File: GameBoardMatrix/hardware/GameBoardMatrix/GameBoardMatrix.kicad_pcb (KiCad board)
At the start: 2 copper layers, 1 part

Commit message: Started on PCB/Schematic Design
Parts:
- removed C1: C, ECE445L:C_Axial_200mil
- added J1: RPI_5_HeaderPins, Connector_PinSocket_2.54mm:PinSocket_2x20_P2.54mm_Vertical, F.Cu at (32.6, 51.2)
- added U1: MUX1, 8to1_MUX:D16, F.Cu at (129.0, 48.4)
- added U2: MUX1, 8to1_MUX:D16, F.Cu at (137.8, 48.4)
- added U3: MUX1, 8to1_MUX:D16, F.Cu at (146.5, 48.4)
- added U4: MUX1, 8to1_MUX:D16, F.Cu at (155.3, 48.4)
- added U5: MUX1, 8to1_MUX:D16, F.Cu at (164.0, 48.4)
- added U6: A3144, A3144HallEffect:1x03_P1.50mm_Vertical_A3144HallEffect, F.Cu at (141.2, 64.2)
- added U7: A3144, A3144HallEffect:1x03_P1.50mm_Vertical_A3144HallEffect, F.Cu at (141.2, 73.0)
- added U8: A3144, A3144HallEffect:1x03_P1.50mm_Vertical_A3144HallEffect, F.Cu at (141.4, 81.5)

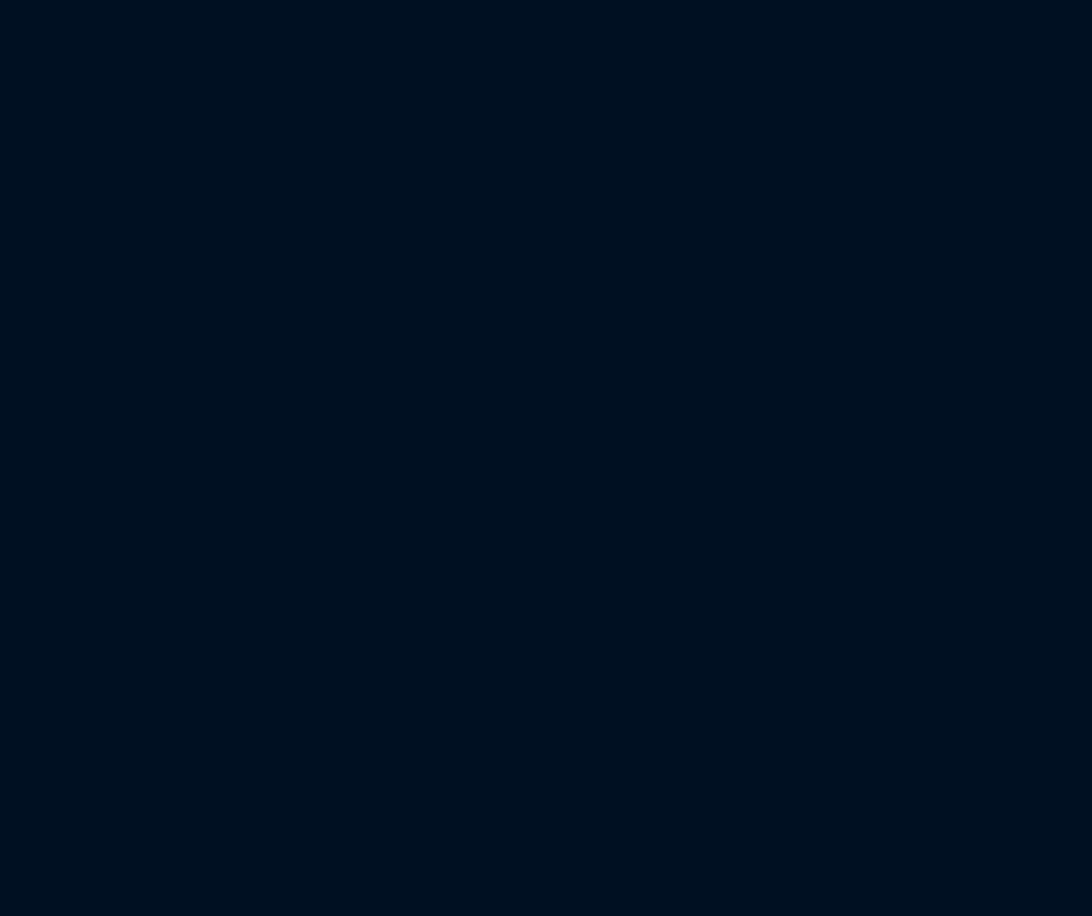
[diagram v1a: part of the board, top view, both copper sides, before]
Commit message: Finished most of the schematic
Still need to tie outputs to gpio pins
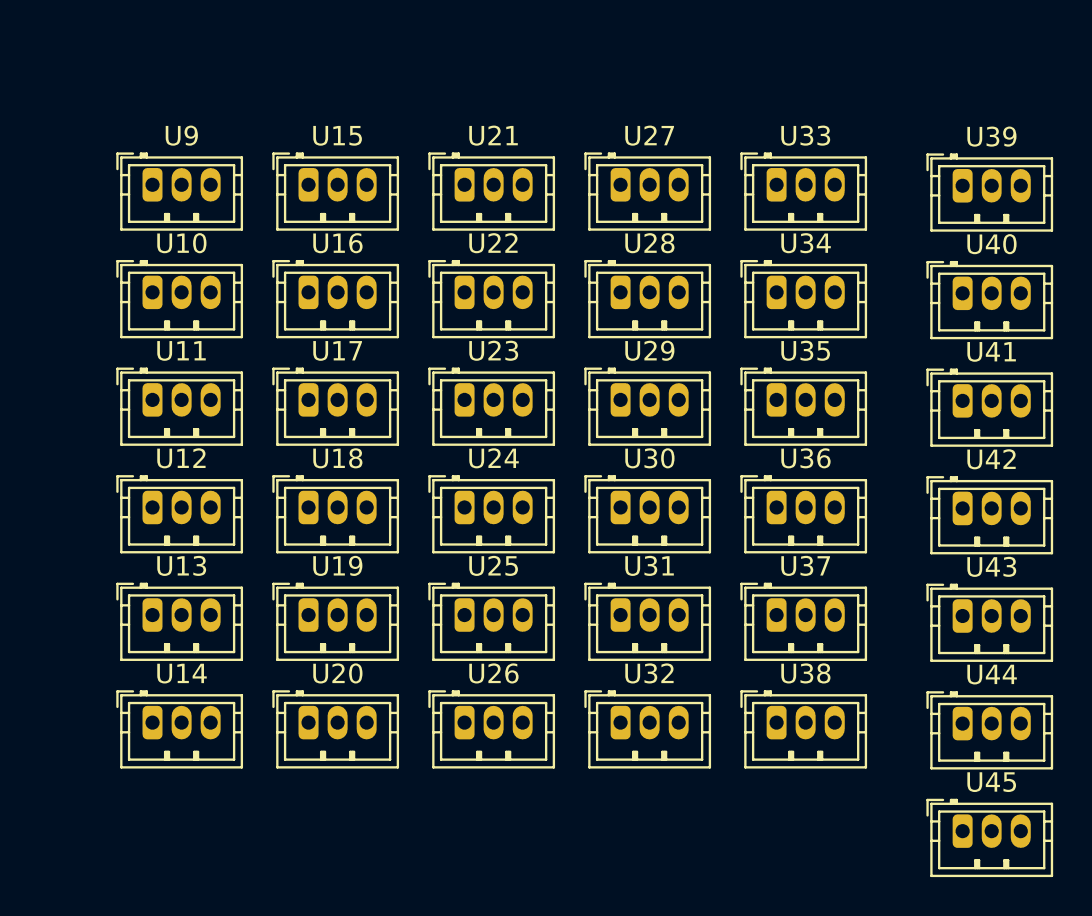
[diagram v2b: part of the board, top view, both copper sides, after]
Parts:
- added U10: A3144, A3144HallEffect:1x03_P1.50mm_Vertical_A3144HallEffect, F.Cu at (172.4, 73.0)
- added U11: A3144, A3144HallEffect:1x03_P1.50mm_Vertical_A3144HallEffect, F.Cu at (172.4, 78.5)
- added U12: A3144, A3144HallEffect:1x03_P1.50mm_Vertical_A3144HallEffect, F.Cu at (172.4, 84.1)
- added U13: A3144, A3144HallEffect:1x03_P1.50mm_Vertical_A3144HallEffect, F.Cu at (172.4, 89.7)
- added U14: A3144, A3144HallEffect:1x03_P1.50mm_Vertical_A3144HallEffect, F.Cu at (172.4, 95.2)
- added U15: A3144, A3144HallEffect:1x03_P1.50mm_Vertical_A3144HallEffect, F.Cu at (180.4, 67.5)
- added U16: A3144, A3144HallEffect:1x03_P1.50mm_Vertical_A3144HallEffect, F.Cu at (180.4, 73.0)
- added U17: A3144, A3144HallEffect:1x03_P1.50mm_Vertical_A3144HallEffect, F.Cu at (180.4, 78.5)
- added U18: A3144, A3144HallEffect:1x03_P1.50mm_Vertical_A3144HallEffect, F.Cu at (180.4, 84.1)
- added U19: A3144, A3144HallEffect:1x03_P1.50mm_Vertical_A3144HallEffect, F.Cu at (180.4, 89.7)
- added U20: A3144, A3144HallEffect:1x03_P1.50mm_Vertical_A3144HallEffect, F.Cu at (180.4, 95.2)
- added U21: A3144, A3144HallEffect:1x03_P1.50mm_Vertical_A3144HallEffect, F.Cu at (188.5, 67.5)
- added U22: A3144, A3144HallEffect:1x03_P1.50mm_Vertical_A3144HallEffect, F.Cu at (188.5, 73.0)
- added U23: A3144, A3144HallEffect:1x03_P1.50mm_Vertical_A3144HallEffect, F.Cu at (188.5, 78.5)
- added U24: A3144, A3144HallEffect:1x03_P1.50mm_Vertical_A3144HallEffect, F.Cu at (188.5, 84.1)
- added U25: A3144, A3144HallEffect:1x03_P1.50mm_Vertical_A3144HallEffect, F.Cu at (188.5, 89.7)
- added U26: A3144, A3144HallEffect:1x03_P1.50mm_Vertical_A3144HallEffect, F.Cu at (188.5, 95.2)
- added U27: A3144, A3144HallEffect:1x03_P1.50mm_Vertical_A3144HallEffect, F.Cu at (196.6, 67.5)
- added U28: A3144, A3144HallEffect:1x03_P1.50mm_Vertical_A3144HallEffect, F.Cu at (196.6, 73.0)
- added U29: A3144, A3144HallEffect:1x03_P1.50mm_Vertical_A3144HallEffect, F.Cu at (196.6, 78.5)
- added U30: A3144, A3144HallEffect:1x03_P1.50mm_Vertical_A3144HallEffect, F.Cu at (196.6, 84.1)
- added U31: A3144, A3144HallEffect:1x03_P1.50mm_Vertical_A3144HallEffect, F.Cu at (196.6, 89.7)
- added U32: A3144, A3144HallEffect:1x03_P1.50mm_Vertical_A3144HallEffect, F.Cu at (196.6, 95.2)
- added U33: A3144, A3144HallEffect:1x03_P1.50mm_Vertical_A3144HallEffect, F.Cu at (204.6, 67.5)
- added U34: A3144, A3144HallEffect:1x03_P1.50mm_Vertical_A3144HallEffect, F.Cu at (204.6, 73.0)
- added U35: A3144, A3144HallEffect:1x03_P1.50mm_Vertical_A3144HallEffect, F.Cu at (204.6, 78.5)
- added U36: A3144, A3144HallEffect:1x03_P1.50mm_Vertical_A3144HallEffect, F.Cu at (204.6, 84.1)
- added U37: A3144, A3144HallEffect:1x03_P1.50mm_Vertical_A3144HallEffect, F.Cu at (204.6, 89.7)
- added U38: A3144, A3144HallEffect:1x03_P1.50mm_Vertical_A3144HallEffect, F.Cu at (204.6, 95.2)
- added U39: A3144, A3144HallEffect:1x03_P1.50mm_Vertical_A3144HallEffect, F.Cu at (214.2, 67.5)
- added U40: A3144, A3144HallEffect:1x03_P1.50mm_Vertical_A3144HallEffect, F.Cu at (214.2, 73.0)
- added U41: A3144, A3144HallEffect:1x03_P1.50mm_Vertical_A3144HallEffect, F.Cu at (214.2, 78.6)
- added U42: A3144, A3144HallEffect:1x03_P1.50mm_Vertical_A3144HallEffect, F.Cu at (214.2, 84.2)
- added U43: A3144, A3144HallEffect:1x03_P1.50mm_Vertical_A3144HallEffect, F.Cu at (214.2, 89.7)
- added U44: A3144, A3144HallEffect:1x03_P1.50mm_Vertical_A3144HallEffect, F.Cu at (214.2, 95.2)
- added U45: A3144, A3144HallEffect:1x03_P1.50mm_Vertical_A3144HallEffect, F.Cu at (214.2, 100.8)
- added U9: A3144, A3144HallEffect:1x03_P1.50mm_Vertical_A3144HallEffect, F.Cu at (172.4, 67.5)
- U1, U2, U3, U4, U5: value MUX1 -> MUX
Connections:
- J1 pad 1: unconnected-(J1-3.3V-Pad1) -> /3.3V_Board
- J1 pad 10: unconnected-(J1-GPIO15-Pad10) -> GPIO15/PIN10
- J1 pad 12: unconnected-(J1-GPIO18-Pad12) -> GPIO18/PIN12
- J1 pad 8: unconnected-(J1-GPIO14-Pad8) -> GPIO14/PIN8
- U1 pad 1: unconnected-(U1-D3-Pad1) -> Net-(U1-D3)
- U1 pad 10: unconnected-(U1-B-Pad10) -> GPIO15/PIN10
- U1 pad 11: unconnected-(U1-A-Pad11) -> GPIO14/PIN8
- U1 pad 12: unconnected-(U1-D7-Pad12) -> Net-(U1-D7)
- U1 pad 13: unconnected-(U1-D6-Pad13) -> Net-(U1-D6)
- U1 pad 14: unconnected-(U1-D5-Pad14) -> Net-(U1-D5)
- U1 pad 15: unconnected-(U1-D4-Pad15) -> Net-(U1-D4)
- U1 pad 16: unconnected-(U1-VCC-Pad16) -> /3.3V_Board
- U1 pad 2: unconnected-(U1-D2-Pad2) -> Net-(U1-D2)
- U1 pad 3: unconnected-(U1-D1-Pad3) -> Net-(U1-D1)
- U1 pad 4: unconnected-(U1-D0-Pad4) -> Net-(U1-D0)
- U1 pad 7: unconnected-(U1-*G-Pad7) -> GND
- U1 pad 8: unconnected-(U1-GND-Pad8) -> GND
- U1 pad 9: unconnected-(U1-C-Pad9) -> GPIO18/PIN12
- U2 pad 1: unconnected-(U2-D3-Pad1) -> Net-(U2-D3)
- U2 pad 10: unconnected-(U2-B-Pad10) -> GPIO15/PIN10
- U2 pad 11: unconnected-(U2-A-Pad11) -> GPIO14/PIN8
- U2 pad 12: unconnected-(U2-D7-Pad12) -> Net-(U2-D7)
- U2 pad 13: unconnected-(U2-D6-Pad13) -> Net-(U2-D6)
- U2 pad 14: unconnected-(U2-D5-Pad14) -> Net-(U18-VOUT)
- U2 pad 15: unconnected-(U2-D4-Pad15) -> Net-(U2-D4)
- U2 pad 16: unconnected-(U2-VCC-Pad16) -> /3.3V_Board
- U2 pad 2: unconnected-(U2-D2-Pad2) -> Net-(U2-D2)
- U2 pad 3: unconnected-(U2-D1-Pad3) -> Net-(U17-VOUT)
- U2 pad 4: unconnected-(U2-D0-Pad4) -> Net-(U2-D0)
- U2 pad 7: unconnected-(U2-*G-Pad7) -> GND
- U2 pad 8: unconnected-(U2-GND-Pad8) -> GND
- U2 pad 9: unconnected-(U2-C-Pad9) -> GPIO18/PIN12
- U3 pad 1: unconnected-(U3-D3-Pad1) -> Net-(U3-D3)
- U3 pad 10: unconnected-(U3-B-Pad10) -> GPIO15/PIN10
- U3 pad 11: unconnected-(U3-A-Pad11) -> GPIO14/PIN8
- U3 pad 12: unconnected-(U3-D7-Pad12) -> Net-(U3-D7)
- U3 pad 13: unconnected-(U3-D6-Pad13) -> Net-(U29-VOUT)
- U3 pad 14: unconnected-(U3-D5-Pad14) -> Net-(U20-VOUT)
- U3 pad 15: unconnected-(U3-D4-Pad15) -> Net-(U11-VOUT)
- U3 pad 16: unconnected-(U3-VCC-Pad16) -> /3.3V_Board
- U3 pad 2: unconnected-(U3-D2-Pad2) -> Net-(U28-VOUT)
- U3 pad 3: unconnected-(U3-D1-Pad3) -> Net-(U19-VOUT)
- U3 pad 4: unconnected-(U3-D0-Pad4) -> Net-(U10-VOUT)
- U3 pad 7: unconnected-(U3-*G-Pad7) -> GND
- U3 pad 8: unconnected-(U3-GND-Pad8) -> GND
- U3 pad 9: unconnected-(U3-C-Pad9) -> GPIO18/PIN12
- U4 pad 1: unconnected-(U4-D3-Pad1) -> Net-(U39-VOUT)
- U4 pad 10: unconnected-(U4-B-Pad10) -> GPIO15/PIN10
- U4 pad 11: unconnected-(U4-A-Pad11) -> GPIO14/PIN8
- U4 pad 12: unconnected-(U4-D7-Pad12) -> Net-(U4-D7)
- U4 pad 13: unconnected-(U4-D6-Pad13) -> Net-(U31-VOUT)
- U4 pad 14: unconnected-(U4-D5-Pad14) -> Net-(U22-VOUT)
- U4 pad 15: unconnected-(U4-D4-Pad15) -> Net-(U13-VOUT)
- U4 pad 16: unconnected-(U4-VCC-Pad16) -> /3.3V_Board
- U4 pad 2: unconnected-(U4-D2-Pad2) -> Net-(U30-VOUT)
- U4 pad 3: unconnected-(U4-D1-Pad3) -> Net-(U21-VOUT)
- U4 pad 4: unconnected-(U4-D0-Pad4) -> Net-(U12-VOUT)
- U4 pad 7: unconnected-(U4-*G-Pad7) -> GND
- U4 pad 8: unconnected-(U4-GND-Pad8) -> GND
- U4 pad 9: unconnected-(U4-C-Pad9) -> GPIO18/PIN12
- U5 pad 1: unconnected-(U5-D3-Pad1) -> Net-(U41-VOUT)
- U5 pad 10: unconnected-(U5-B-Pad10) -> GPIO15/PIN10
- U5 pad 11: unconnected-(U5-A-Pad11) -> GPIO14/PIN8
- U5 pad 12: unconnected-(U5-D7-Pad12) -> Net-(U45-VOUT)
- U5 pad 13: unconnected-(U5-D6-Pad13) -> Net-(U44-VOUT)
- U5 pad 14: unconnected-(U5-D5-Pad14) -> Net-(U43-VOUT)
- U5 pad 15: unconnected-(U5-D4-Pad15) -> Net-(U42-VOUT)
- U5 pad 16: unconnected-(U5-VCC-Pad16) -> /3.3V_Board
- U5 pad 2: unconnected-(U5-D2-Pad2) -> Net-(U32-VOUT)
- U5 pad 3: unconnected-(U5-D1-Pad3) -> Net-(U23-VOUT)
- U5 pad 4: unconnected-(U5-D0-Pad4) -> Net-(U14-VOUT)
- U5 pad 8: unconnected-(U5-GND-Pad8) -> GND
- U5 pad 9: unconnected-(U5-C-Pad9) -> GPIO18/PIN12
- U6 pad 1: unconnected-(U6-VCC-Pad1) -> /3.3V_Board
- U6 pad 2: unconnected-(U6-VOUT-Pad2) -> Net-(U1-D0)
- U6 pad 3: unconnected-(U6-GND-Pad3) -> GND
- U7 pad 1: unconnected-(U7-VCC-Pad1) -> /3.3V_Board
- U7 pad 2: unconnected-(U7-VOUT-Pad2) -> Net-(U1-D4)
- U7 pad 3: unconnected-(U7-GND-Pad3) -> GND
- U8 pad 1: unconnected-(U8-VCC-Pad1) -> /3.3V_Board
- U8 pad 2: unconnected-(U8-VOUT-Pad2) -> Net-(U2-D0)
- U8 pad 3: unconnected-(U8-GND-Pad3) -> GND

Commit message: %50 done with PCB
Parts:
- added C1: 0.1uF, footprints:CAP_CL21_SAM-M, F.Cu at (59.1, 42.2)
- added C10: 0.1uF, footprints:CAP_CL21_SAM-M, F.Cu at (80.4, 52.2)
- added C11: 0.1uF, footprints:CAP_CL21_SAM-M, F.Cu at (80.4, 62.6)
- added C12: 0.1uF, footprints:CAP_CL21_SAM-M, F.Cu at (80.4, 71.6)
- added C13: 0.1uF, footprints:CAP_CL21_SAM-M, F.Cu at (91.4, 82.0)
- added C14: 0.1uF, footprints:CAP_CL21_SAM-M, F.Cu at (91.4, 92.0)
- added C15: 0.1uF, footprints:CAP_CL21_SAM-M, F.Cu at (91.6, 102.2)
- added C16: 0.1uF, footprints:CAP_CL21_SAM-M, F.Cu at (91.4, 111.6)
- added C17: 0.1uF, footprints:CAP_CL21_SAM-M, F.Cu at (103.6, 42.0)
- added C18: 0.1uF, footprints:CAP_CL21_SAM-M, F.Cu at (103.6, 51.6)
- added C19: 0.1uF, footprints:CAP_CL21_SAM-M, F.Cu at (103.6, 60.8)
- added C2: 0.1uF, footprints:CAP_CL21_SAM-M, F.Cu at (70.6, 80.2)
- added C20: 0.1uF, footprints:CAP_CL21_SAM-M, F.Cu at (103.4, 72.0)
- added C21: 0.1uF, footprints:CAP_CL21_SAM-M, F.Cu at (114.4, 82.2)
- added C22: 0.1uF, footprints:CAP_CL21_SAM-M, F.Cu at (114.4, 91.4)
- added C23: 0.1uF, footprints:CAP_CL21_SAM-M, F.Cu at (114.6, 101.2)
- added C24: 0.1uF, footprints:CAP_CL21_SAM-M, F.Cu at (114.6, 111.4)
- added C25: 0.1uF, footprints:CAP_CL21_SAM-M, F.Cu at (125.2, 41.2)
- added C26: 0.1uF, footprints:CAP_CL21_SAM-M, F.Cu at (125.2, 51.2)
- added C27: 0.1uF, footprints:CAP_CL21_SAM-M, F.Cu at (125.2, 61.0)
- added C28: 0.1uF, footprints:CAP_CL21_SAM-M, F.Cu at (125.2, 70.4)
- added C29: 0.1uF, footprints:CAP_CL21_SAM-M, F.Cu at (135.8, 81.4)
- added C3: 0.1uF, footprints:CAP_CL21_SAM-M, F.Cu at (59.2, 52.0)
- added C30: 0.1uF, footprints:CAP_CL21_SAM-M, F.Cu at (135.4, 91.4)
- added C31: 0.1uF, footprints:CAP_CL21_SAM-M, F.Cu at (135.2, 100.8)
- added C32: 0.1uF, footprints:CAP_CL21_SAM-M, F.Cu at (135.2, 110.6)
- added C33: 0.1uF, footprints:CAP_CL21_SAM-M, F.Cu at (148.6, 40.6)
- added C34: 0.1uF, footprints:CAP_CL21_SAM-M, F.Cu at (148.6, 50.2)
- added C35: 0.1uF, footprints:CAP_CL21_SAM-M, F.Cu at (148.6, 60.4)
- added C36: 0.1uF, footprints:CAP_CL21_SAM-M, F.Cu at (148.6, 70.0)
- added C37: 0.1uF, footprints:CAP_CL21_SAM-M, F.Cu at (159.8, 82.0)
- added C38: 0.1uF, footprints:CAP_CL21_SAM-M, F.Cu at (160.0, 92.0)
- added C39: 0.1uF, footprints:CAP_CL21_SAM-M, F.Cu at (160.0, 102.0)
- added C4: 0.1uF, footprints:CAP_CL21_SAM-M, F.Cu at (59.0, 61.8)
- added C40: 0.1uF, footprints:CAP_CL21_SAM-M, F.Cu at (160.0, 111.6)
- added C41: 4.7uF, Capacitor_THT:CP_Axial_L10.0mm_D4.5mm_P15.00mm_Horizontal, F.Cu at (26.3, 25.2)
- added C42: 4.7uF, Capacitor_THT:CP_Axial_L10.0mm_D4.5mm_P15.00mm_Horizontal, F.Cu at (41.5, 32.0)
- added C5: 0.1uF, footprints:CAP_CL21_SAM-M, F.Cu at (59.0, 71.4)
- added C6: 0.1uF, footprints:CAP_CL21_SAM-M, F.Cu at (70.6, 89.4)
- added C7: 0.1uF, footprints:CAP_CL21_SAM-M, F.Cu at (70.6, 99.8)
- added C8: 0.1uF, footprints:CAP_CL21_SAM-M, F.Cu at (70.2, 109.6)
- added C9: 0.1uF, footprints:CAP_CL21_SAM-M, F.Cu at (80.2, 42.8)
- added IC1: LM2937ET-3.3_NOPB, ECE445L:TO254P470X1028X1955-3P, F.Cu at (28.5, 39.2)
- added R1: 10k, ECE445L:R_Axial_DIN0204_L3.6mm_D1.6mm_P7.62mm_Horizontal, F.Cu at (71.0, 38.8)
- added R10: 10k, ECE445L:R_Axial_DIN0204_L3.6mm_D1.6mm_P7.62mm_Horizontal, F.Cu at (92.2, 48.8)
- added R11: 10k, ECE445L:R_Axial_DIN0204_L3.6mm_D1.6mm_P7.62mm_Horizontal, F.Cu at (92.2, 58.6)
- added R12: 10k, ECE445L:R_Axial_DIN0204_L3.6mm_D1.6mm_P7.62mm_Horizontal, F.Cu at (92.2, 68.4)
- added R13: 10k, ECE445L:R_Axial_DIN0204_L3.6mm_D1.6mm_P7.62mm_Horizontal, F.Cu at (79.4, 85.8)
- added R14: 10k, ECE445L:R_Axial_DIN0204_L3.6mm_D1.6mm_P7.62mm_Horizontal, F.Cu at (79.4, 95.6)
- added R15: 10k, ECE445L:R_Axial_DIN0204_L3.6mm_D1.6mm_P7.62mm_Horizontal, F.Cu at (79.4, 105.6)
- added R16: 10k, ECE445L:R_Axial_DIN0204_L3.6mm_D1.6mm_P7.62mm_Horizontal, F.Cu at (79.4, 115.4)
- added R17: 10k, ECE445L:R_Axial_DIN0204_L3.6mm_D1.6mm_P7.62mm_Horizontal, F.Cu at (115.4, 38.4)
- added R18: 10k, ECE445L:R_Axial_DIN0204_L3.6mm_D1.6mm_P7.62mm_Horizontal, F.Cu at (115.4, 48.2)
- added R19: 10k, ECE445L:R_Axial_DIN0204_L3.6mm_D1.6mm_P7.62mm_Horizontal, F.Cu at (115.4, 58.0)
- added R2: 10k, ECE445L:R_Axial_DIN0204_L3.6mm_D1.6mm_P7.62mm_Horizontal, F.Cu at (58.6, 84.4)
- added R20: 10k, ECE445L:R_Axial_DIN0204_L3.6mm_D1.6mm_P7.62mm_Horizontal, F.Cu at (115.4, 67.8)
- added R21: 10k, ECE445L:R_Axial_DIN0204_L3.6mm_D1.6mm_P7.62mm_Horizontal, F.Cu at (102.8, 85.0)
- added R22: 10k, ECE445L:R_Axial_DIN0204_L3.6mm_D1.6mm_P7.62mm_Horizontal, F.Cu at (102.8, 94.8)
- added R23: 10k, ECE445L:R_Axial_DIN0204_L3.6mm_D1.6mm_P7.62mm_Horizontal, F.Cu at (102.8, 104.6)
- added R24: 10k, ECE445L:R_Axial_DIN0204_L3.6mm_D1.6mm_P7.62mm_Horizontal, F.Cu at (102.8, 114.4)
- added R25: 10k, ECE445L:R_Axial_DIN0204_L3.6mm_D1.6mm_P7.62mm_Horizontal, F.Cu at (137.2, 37.8)
- added R26: 10k, ECE445L:R_Axial_DIN0204_L3.6mm_D1.6mm_P7.62mm_Horizontal, F.Cu at (137.2, 47.6)
- added R27: 10k, ECE445L:R_Axial_DIN0204_L3.6mm_D1.6mm_P7.62mm_Horizontal, F.Cu at (137.2, 57.4)
- added R28: 10k, ECE445L:R_Axial_DIN0204_L3.6mm_D1.6mm_P7.62mm_Horizontal, F.Cu at (137.2, 67.2)
- added R29: 10k, ECE445L:R_Axial_DIN0204_L3.6mm_D1.6mm_P7.62mm_Horizontal, F.Cu at (123.2, 85.0)
- added R3: 10k, ECE445L:R_Axial_DIN0204_L3.6mm_D1.6mm_P7.62mm_Horizontal, F.Cu at (71.0, 48.6)
- added R30: 10k, ECE445L:R_Axial_DIN0204_L3.6mm_D1.6mm_P7.62mm_Horizontal, F.Cu at (123.2, 94.8)
- added R31: 10k, ECE445L:R_Axial_DIN0204_L3.6mm_D1.6mm_P7.62mm_Horizontal, F.Cu at (123.2, 104.6)
- added R32: 10k, ECE445L:R_Axial_DIN0204_L3.6mm_D1.6mm_P7.62mm_Horizontal, F.Cu at (123.2, 114.4)
- added R33: 10k, ECE445L:R_Axial_DIN0204_L3.6mm_D1.6mm_P7.62mm_Horizontal, F.Cu at (160.4, 37.4)
- added R34: 10k, ECE445L:R_Axial_DIN0204_L3.6mm_D1.6mm_P7.62mm_Horizontal, F.Cu at (160.4, 47.2)
- added R35: 10k, ECE445L:R_Axial_DIN0204_L3.6mm_D1.6mm_P7.62mm_Horizontal, F.Cu at (160.4, 57.0)
- added R36: 10k, ECE445L:R_Axial_DIN0204_L3.6mm_D1.6mm_P7.62mm_Horizontal, F.Cu at (160.4, 66.8)
- added R37: 10k, ECE445L:R_Axial_DIN0204_L3.6mm_D1.6mm_P7.62mm_Horizontal, F.Cu at (148.0, 86.0)
- added R38: 10k, ECE445L:R_Axial_DIN0204_L3.6mm_D1.6mm_P7.62mm_Horizontal, F.Cu at (148.0, 95.8)
- added R39: 10k, ECE445L:R_Axial_DIN0204_L3.6mm_D1.6mm_P7.62mm_Horizontal, F.Cu at (148.0, 105.6)
- added R4: 10k, ECE445L:R_Axial_DIN0204_L3.6mm_D1.6mm_P7.62mm_Horizontal, F.Cu at (71.0, 58.4)
- added R40: 10k, ECE445L:R_Axial_DIN0204_L3.6mm_D1.6mm_P7.62mm_Horizontal, F.Cu at (148.0, 115.4)
- added R5: 10k, ECE445L:R_Axial_DIN0204_L3.6mm_D1.6mm_P7.62mm_Horizontal, F.Cu at (71.0, 68.2)
- added R6: 10k, ECE445L:R_Axial_DIN0204_L3.6mm_D1.6mm_P7.62mm_Horizontal, F.Cu at (58.6, 94.2)
- added R7: 10k, ECE445L:R_Axial_DIN0204_L3.6mm_D1.6mm_P7.62mm_Horizontal, F.Cu at (58.6, 104.0)
- added R8: 10k, ECE445L:R_Axial_DIN0204_L3.6mm_D1.6mm_P7.62mm_Horizontal, F.Cu at (58.6, 113.8)
- added R9: 10k, ECE445L:R_Axial_DIN0204_L3.6mm_D1.6mm_P7.62mm_Horizontal, F.Cu at (92.2, 39.0)
- added TP1: TP, ECE445L:Testpoint_1x02_P2.54mm, F.Cu at (56.0, 29.5)
- added TP2: TP, ECE445L:Testpoint_1x02_P2.54mm, F.Cu at (76.4, 28.9)
- added TP3: TP, ECE445L:Testpoint_1x02_P2.54mm, F.Cu at (101.2, 28.9)
- added TP4: TP, ECE445L:Testpoint_1x02_P2.54mm, F.Cu at (123.4, 28.3)
- added TP5: TP, ECE445L:Testpoint_1x02_P2.54mm, F.Cu at (146.8, 28.1)
- added TP6: TP, ECE445L:Testpoint_1x02_P2.54mm, F.Cu at (52.6, 40.9)
- added TP7: TP, ECE445L:Testpoint_1x02_P2.54mm, F.Cu at (41.2, 38.1)
- J1: moved to B.Cu
- U17, U27, U37, U7: value A3144 -> MUX; footprint A3144HallEffect:1x03_P1.50mm_Vertical_A3144HallEffect -> 8to1_MUX:D16
- U2, U3, U4, U5: value MUX -> A3144; footprint 8to1_MUX:D16 -> A3144HallEffect:1x03_P1.50mm_Vertical_A3144HallEffect
- moved U33 140.5 mm to (64.2, 73.0), turned to 90 degrees
- moved U24 126.0 mm to (64.2, 63.4), turned to 90 degrees
- moved U15 116.9 mm to (64.4, 53.6), turned to 90 degrees
- moved U5 115.9 mm to (65.2, 108.8), turned to -90 degrees
- moved U4 103.1 mm to (65.3, 98.8), turned to -90 degrees
- moved U16 101.1 mm to (86.2, 109.6), turned to -90 degrees
- moved U3 90.4 mm to (65.4, 88.3), turned to -90 degrees
- moved U9 87.9 mm to (85.6, 53.8), turned to 90 degrees
- moved U10 87.2 mm to (85.6, 64.4), turned to 90 degrees
- moved U11 87.0 mm to (85.6, 73.2), turned to 90 degrees
- moved U17 86.4 mm to (109.4, 29.5)
- moved U12 86.3 mm to (86.2, 80.0), turned to -90 degrees
- moved U13 86.2 mm to (86.2, 90.0), turned to -90 degrees
- moved U14 86.1 mm to (86.4, 100.2), turned to -90 degrees
- moved U18 82.2 mm to (108.8, 43.8), turned to 90 degrees
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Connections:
- J1 pad 1: /3.3V_Board -> unconnected-(J1-3.3V-Pad1)
- J1 pad 11: unconnected-(J1-GPIO17-Pad11) -> GPIO17/PIN11
- J1 pad 13: unconnected-(J1-GPIO27-Pad13) -> GPIO27/PIN15
- J1 pad 14: unconnected-(J1-GND-Pad14) -> GND
- J1 pad 2: unconnected-(J1-5V-Pad2) -> 5V Board
- J1 pad 20: unconnected-(J1-GND-Pad20) -> GND
- J1 pad 3: unconnected-(J1-GPIO2-Pad3) -> GPIO2/PIN3
- J1 pad 34: unconnected-(J1-GND-Pad34) -> GND
- J1 pad 39: unconnected-(J1-GND-Pad39) -> GND
- J1 pad 5: unconnected-(J1-GPIO3-Pad5) -> GPIO3/PIN5
- J1 pad 6: unconnected-(J1-GND-Pad6) -> GND
- J1 pad 7: unconnected-(J1-GPIO4-Pad7) -> GPIO4/PIN7
- J1 pad 9: unconnected-(J1-GND-Pad9) -> GND
- U1 pad 6: unconnected-(U1-W-Pad6) -> GPIO2/PIN3
- U16 pad 2: Net-(U1-D5) -> Net-(U16-VOUT)
- U17 pad 1: /3.3V_Board -> Net-(U17-D3)
- U17 pad 2: Net-(U17-VOUT) -> Net-(U17-D2)
- U17 pad 3: GND -> Net-(U17-D1)
- U18 pad 2: Net-(U18-VOUT) -> Net-(U17-D0)
- U19 pad 2: Net-(U19-VOUT) -> Net-(U17-D1)
- U2 pad 1: Net-(U2-D3) -> /3.3V_Board
- U2 pad 2: Net-(U2-D2) -> Net-(U1-D4)
- U2 pad 3: Net-(U17-VOUT) -> GND
- U20 pad 2: Net-(U20-VOUT) -> Net-(U17-D2)
- U21 pad 2: Net-(U21-VOUT) -> Net-(U17-D3)
- U22 pad 2: Net-(U22-VOUT) -> Net-(U17-D4)
- U23 pad 2: Net-(U23-VOUT) -> Net-(U17-D5)
- U25 pad 2: Net-(U1-D6) -> Net-(U17-D6)
- U26 pad 2: Net-(U2-D2) -> Net-(U17-D7)
- U27 pad 1: /3.3V_Board -> Net-(U27-D3)
- U27 pad 2: Net-(U2-D6) -> Net-(U27-D2)
- U27 pad 3: GND -> Net-(U27-D1)
- U28 pad 2: Net-(U28-VOUT) -> Net-(U27-D0)
- U29 pad 2: Net-(U29-VOUT) -> Net-(U27-D1)
- U3 pad 1: Net-(U3-D3) -> /3.3V_Board
- U3 pad 2: Net-(U28-VOUT) -> Net-(U1-D5)
- U3 pad 3: Net-(U19-VOUT) -> GND
- U30 pad 2: Net-(U30-VOUT) -> Net-(U27-D2)
- U31 pad 2: Net-(U31-VOUT) -> Net-(U27-D3)
- U32 pad 2: Net-(U32-VOUT) -> Net-(U27-D4)
- U34 pad 2: Net-(U1-D7) -> Net-(U27-D5)
- U35 pad 2: Net-(U2-D3) -> Net-(U27-D6)
- U36 pad 2: Net-(U2-D7) -> Net-(U27-D7)
- U37 pad 1: /3.3V_Board -> Net-(U37-D3)
- U37 pad 2: Net-(U3-D3) -> Net-(U37-D2)
- U37 pad 3: GND -> Net-(U37-D1)
- U38 pad 2: Net-(U3-D7) -> Net-(U37-D0)
- U39 pad 2: Net-(U39-VOUT) -> Net-(U37-D1)
- U4 pad 1: Net-(U39-VOUT) -> /3.3V_Board
- U4 pad 2: Net-(U30-VOUT) -> Net-(U1-D6)
- U4 pad 3: Net-(U21-VOUT) -> GND
- U40 pad 2: Net-(U4-D7) -> Net-(U37-D2)
- U41 pad 2: Net-(U41-VOUT) -> Net-(U37-D3)
- U42 pad 2: Net-(U42-VOUT) -> Net-(U37-D4)
- U43 pad 2: Net-(U43-VOUT) -> Net-(U37-D5)
- U44 pad 2: Net-(U44-VOUT) -> Net-(U37-D6)
- U45 pad 2: Net-(U45-VOUT) -> Net-(U37-D7)
- U5 pad 1: Net-(U41-VOUT) -> /3.3V_Board
- U5 pad 2: Net-(U32-VOUT) -> Net-(U1-D7)
- U5 pad 3: Net-(U23-VOUT) -> GND
- U7 pad 1: /3.3V_Board -> Net-(U11-VOUT)
- U7 pad 2: Net-(U1-D4) -> Net-(U10-VOUT)
- U7 pad 3: GND -> Net-(U7-D1)
- U8 pad 2: Net-(U2-D0) -> Net-(U7-D0)
- U9 pad 2: Net-(U2-D4) -> Net-(U7-D1)
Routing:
- net GPIO18/PIN12: track 0.00 -> 214.7 mm, vias 0 -> 8
- net GPIO15/PIN10: track 0.00 -> 210.8 mm, vias 0 -> 8
- net GPIO14/PIN8: track 0.00 -> 207.3 mm, vias 0 -> 8
- net GPIO27/PIN15: track 0.00 -> 179.2 mm
- net GPIO17/PIN11: track 0.00 -> 152.4 mm
- net GPIO4/PIN7: track 0.00 -> 124.3 mm
- net /3.3V_Board: track 0.00 -> 118.6 mm
- net GND: track 0.00 -> 115.3 mm
- net GPIO3/PIN5: track 0.00 -> 96.0 mm
- net GPIO2/PIN3: track 0.00 -> 80.2 mm, vias 0 -> 2
- net 5V Board: track 0.00 -> 31.2 mm
- net Net-(TP6-A): track 0.00 -> 24.6 mm
- net Net-(U17-D3): track 0.00 -> 8.13 mm
- net Net-(U1-D5): track 0.00 -> 8.01 mm
- net Net-(U10-VOUT): track 0.00 -> 7.76 mm
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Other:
- board outline added: 150 x 100 mm
- board text added: "Game Board PCB"

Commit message: duck
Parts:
- added ?: , , F.Cu at (168.5, 114.5)
- added ?: , , F.Cu at (168.5, 18.2)
- added ?: , , F.Cu at (25.2, 17.0)
- added REF**: MountingHole_6.5mm, MountingHole:MountingHole_6.5mm, F.Cu at (27.2, 112.5)
- moved TP1 12.5 mm to (66.1, 36.8), turned to -90 degrees
- moved TP5 2.40 mm to (144.4, 28.3)
- moved TP4 1.77 mm to (121.8, 29.0)
- moved TP6 0.21 mm to (52.6, 40.7)
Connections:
- C1 pad 2: GND -> GND2
- C10 pad 2: GND -> GND2
- C11 pad 2: GND -> GND2
- C12 pad 2: GND -> GND2
- C13 pad 2: GND -> GND2
- C14 pad 2: GND -> GND2
- C15 pad 2: GND -> GND2
- C16 pad 2: GND -> GND2
- C17 pad 2: GND -> GND2
- C18 pad 2: GND -> GND2
- C19 pad 2: GND -> GND2
- C2 pad 2: GND -> GND2
- C20 pad 2: GND -> GND2
- C21 pad 2: GND -> GND2
- C22 pad 2: GND -> GND2
- C23 pad 2: GND -> GND2
- C24 pad 2: GND -> GND2
- C25 pad 2: GND -> GND2
- C26 pad 2: GND -> GND2
- C27 pad 2: GND -> GND2
- C28 pad 2: GND -> GND2
- C29 pad 2: GND -> GND2
- C3 pad 2: GND -> GND2
- C30 pad 2: GND -> GND2
- C31 pad 2: GND -> GND2
- C32 pad 2: GND -> GND2
- C33 pad 2: GND -> GND2
- C34 pad 2: GND -> GND2
- C35 pad 2: GND -> GND2
- C36 pad 2: GND -> GND2
- C37 pad 2: GND -> GND2
- C38 pad 2: GND -> GND2
- C39 pad 2: GND -> GND2
- C4 pad 2: GND -> GND2
- C40 pad 2: GND -> GND2
- C41 pad 2: GND -> GND3
- C42 pad 2: GND -> GND3
- C5 pad 2: GND -> GND2
- C6 pad 2: GND -> GND2
- C7 pad 2: GND -> GND2
- C8 pad 2: GND -> GND2
- C9 pad 2: GND -> GND2
- IC1 pad 2: GND -> GND3
- J1 pad 14: GND -> unconnected-(J1-GND-Pad14)
- J1 pad 20: GND -> unconnected-(J1-GND-Pad20)
- J1 pad 25: unconnected-(J1-GND-Pad25) -> GND
- J1 pad 34: GND -> unconnected-(J1-GND-Pad34)
- J1 pad 39: GND -> GND2
- J1 pad 6: GND -> GND3
- J1 pad 9: GND -> unconnected-(J1-GND-Pad9)
- TP6 pad 2: GND -> GND2
- U10 pad 3: GND -> GND2
- U11 pad 3: GND -> GND2
- U12 pad 3: GND -> GND2
- U13 pad 3: GND -> GND2
- U14 pad 3: GND -> GND2
- U15 pad 3: GND -> GND2
- U16 pad 3: GND -> GND2
- U18 pad 3: GND -> GND2
- U19 pad 3: GND -> GND2
- U2 pad 3: GND -> GND2
- U20 pad 3: GND -> GND2
- U21 pad 3: GND -> GND2
- U22 pad 3: GND -> GND2
- U23 pad 3: GND -> GND2
- U24 pad 3: GND -> GND2
- U25 pad 3: GND -> GND2
- U26 pad 3: GND -> GND2
- U28 pad 3: GND -> GND2
- U29 pad 3: GND -> GND2
- U3 pad 3: GND -> GND2
- U30 pad 3: GND -> GND2
- U31 pad 3: GND -> GND2
- U32 pad 3: GND -> GND2
- U33 pad 3: GND -> GND2
- U34 pad 3: GND -> GND2
- U35 pad 3: GND -> GND2
- U36 pad 3: GND -> GND2
- U38 pad 3: GND -> GND2
- U39 pad 3: GND -> GND2
- U4 pad 3: GND -> GND2
- U40 pad 3: GND -> GND2
- U41 pad 3: GND -> GND2
- U42 pad 3: GND -> GND2
- U43 pad 3: GND -> GND2
- U44 pad 3: GND -> GND2
- U45 pad 3: GND -> GND2
- U5 pad 3: GND -> GND2
- U6 pad 3: GND -> GND2
- U8 pad 3: GND -> GND2
- U9 pad 3: GND -> GND2
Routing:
- net /3.3V_Board: track 118.6 -> 1062.2 mm, vias 0 -> 9
- net GND2: track 0.00 -> 752.7 mm
- net GND: track 115.3 -> 228.4 mm, vias 0 -> 6
- net Net-(U16-VOUT): track 0.00 -> 104.1 mm
- net Net-(U37-D7): track 0.00 -> 101.3 mm
- net Net-(U27-D7): track 0.00 -> 101.2 mm
- net Net-(U14-VOUT): track 0.00 -> 95.1 mm, vias 0 -> 2
- net Net-(U1-D7): track 7.43 -> 102.4 mm, vias 0 -> 2
- net Net-(U37-D6): track 0.00 -> 93.4 mm, vias 0 -> 2
- net Net-(U17-D7): track 7.44 -> 100.9 mm
- net Net-(U27-D6): track 0.00 -> 93.1 mm, vias 0 -> 2
- net Net-(U1-D6): track 7.67 -> 93.7 mm, vias 0 -> 2
- net Net-(U27-D5): track 0.00 -> 85.9 mm, vias 0 -> 2
- net Net-(U37-D5): track 0.00 -> 85.9 mm, vias 0 -> 2
- net Net-(U13-VOUT): track 0.00 -> 85.8 mm, vias 0 -> 2
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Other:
- board size 150 x 100 mm -> 153.3 x 107.2 mm
- board text added: "PCB of Treachery - 2024 v1.0 Luis Duarte Gonzalez Iniyan Ilangovan Lizette Wong Jrnna Jacobs Ollie Radek Thu Nguyen UTX_464D"

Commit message: Added order details
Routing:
- net 5V Board: track 31.2 -> 31.7 mm
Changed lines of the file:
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@@
 			(outputformat 1)
 			(mirror no)
-			(drillshape 1)
+			(drillshape 0)
 			(scaleselection 1)
-			(outputdirectory "")
+			(outputdirectory "../GameBoardGerber/")
 		)
 	)
@@
 		)
 		(property "Footprint" "footprints:CAP_CL21_SAM-M"
-			(at 0 0 -90)
+			(at 0 0 90)
 			(layer "F.Fab")
 			(hide yes)
@@
 		)
 		(property "Datasheet" ""
-			(at 0 0 -90)
+			(at 0 0 90)
 			(layer "F.Fab")
 			(hide yes)
@@
 		)
 		(property "Description" "Unpolarized capacitor"
-			(at 0 0 -90)
+			(at 0 0 90)
 			(layer "F.Fab")
 			(hide yes)
@@
 		)
 		(fp_text user "${REFERENCE}"
-			(at 0 1.27 360)
+			(at 0 1.27 0)
 			(layer "F.Fab")
 			(effects
@@
 	)
 	(segment
-		(start 34.34 53.12)
+		(start 28.46 47.24)
+		(end 28.46 39.25)
+		(width 0.5)
+		(layer "F.Cu")
+		(net 79)
+	)
+	(segment
+		(start 31.485 50.265)
 		(end 28.46 47.24)
 		(width 0.5)
@@
 	)
 	(segment
-		(start 28.46 47.24)
-		(end 28.46 39.25)
+		(start 31.485 50.265)
+		(end 31.86 50.64)
 		(width 0.5)
 		(layer "F.Cu")
@@
 		(width 0.5)
 		(layer "F.Cu")
+		(net 79)
+	)
+	(segment
+		(start 34.34 53.12)
+		(end 31.485 50.265)
+		(width 0.5)
+		(layer "F.Cu")
